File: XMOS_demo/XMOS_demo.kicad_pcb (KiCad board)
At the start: 2 copper layers, 100 x 100 mm, 128 parts, among them J1 XSYS2 DEBUG CONNECTOR, J2 USB_C_Receptacle_USB2.0_16P, J3 AudioJack3_SwitchT, U1 U316-1024-QF60B, U2 CS4271, U3 AP61200Z6, U4 TPD3S014, U5 MAX97220C, U6 W25Q32JVSS, Y1 Crystal_24M, Y2 24.576M

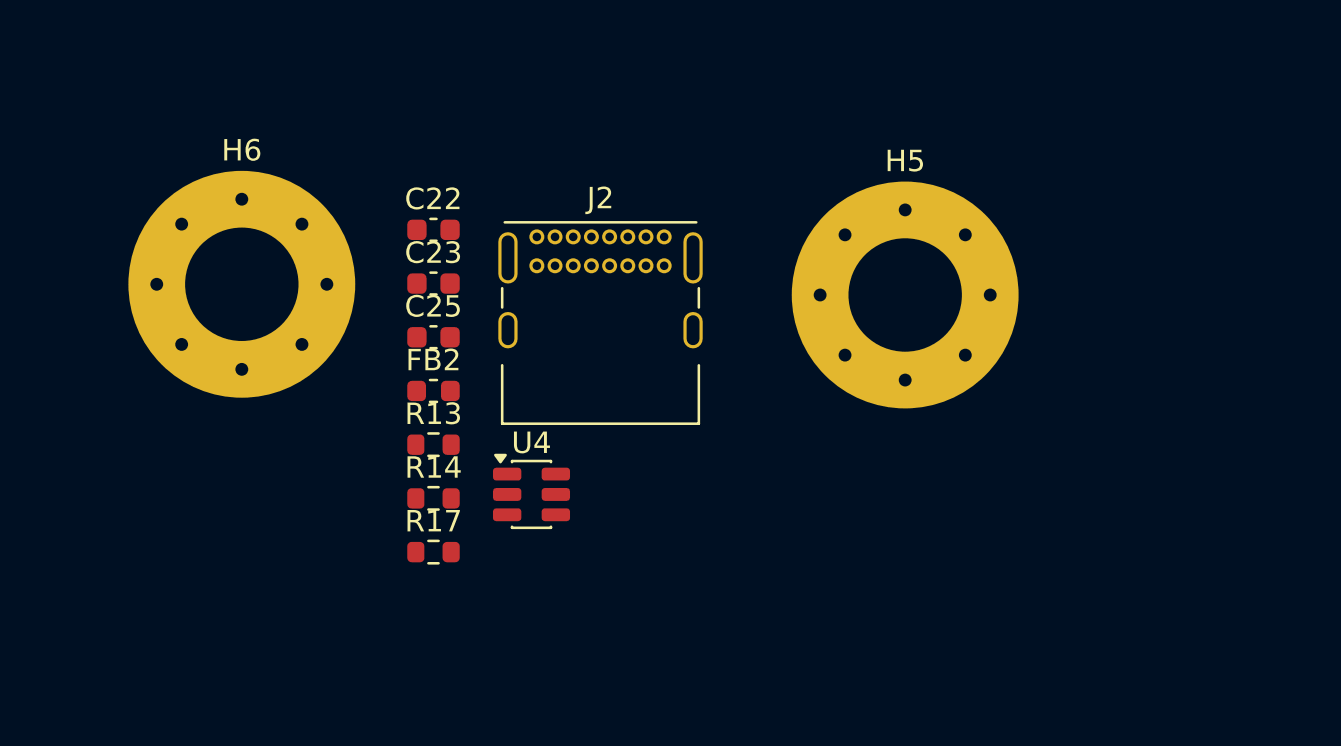
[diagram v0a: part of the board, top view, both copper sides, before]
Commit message: terminal block for power input added
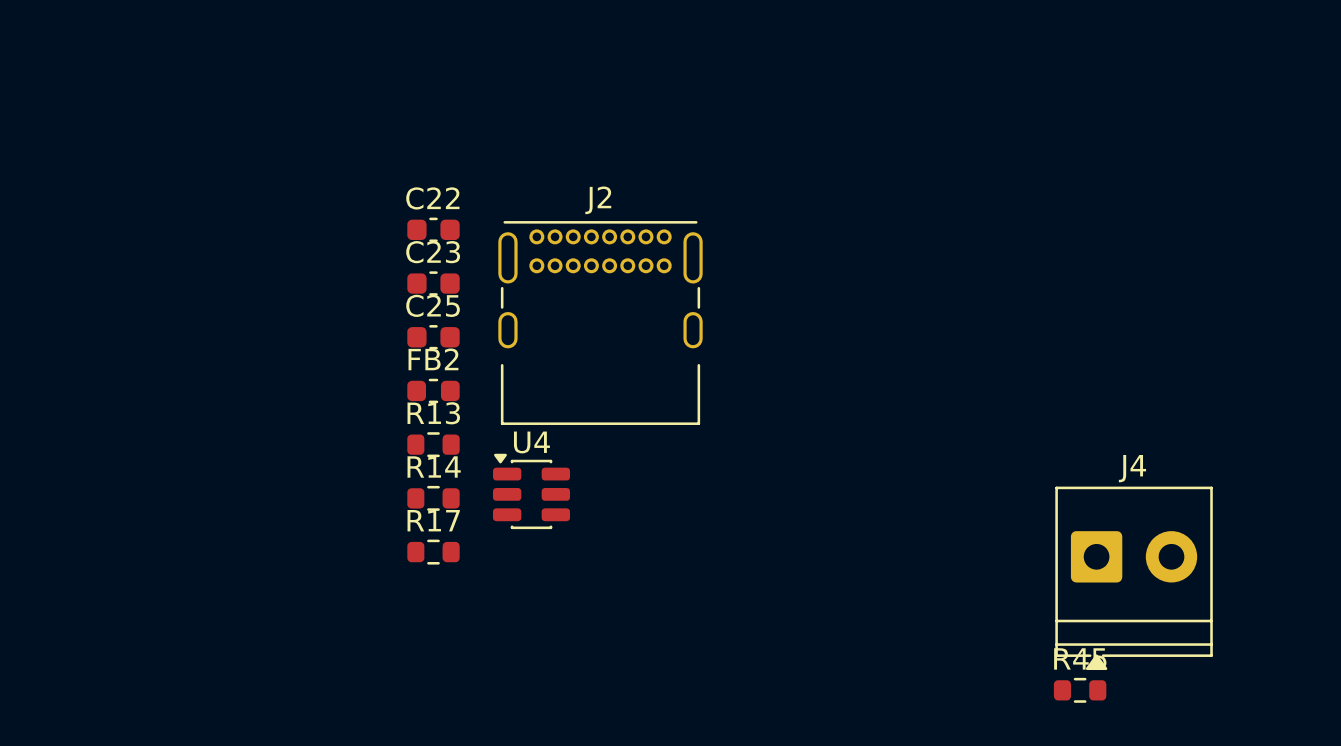
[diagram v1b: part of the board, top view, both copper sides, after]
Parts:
- removed H5: VBUS, MountingHole:MountingHole_5.3mm_M5_Pad_Via
- removed H6: GND, MountingHole:MountingHole_5.3mm_M5_Pad_Via
- added J4: Screw_Terminal_P3.50mm, TerminalBlock_Phoenix:TerminalBlock_Phoenix_PT-1,5-2-3.5-H_1x02_P3.50mm_Horizontal, F.Cu at (161.9, 181.8)
- added R45: 0R3, Resistor_SMD:R_0603_1608Metric, F.Cu at (161.2, 188.0)

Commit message: sch mostly finished, needs tp, pcb component layout started
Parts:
- removed the R17 at (131.0, 181.5)
- added C24: 22u, Capacitor_SMD:C_1206_3216Metric, F.Cu at (223.4, 126.6)
- added C26: 22u, Capacitor_SMD:C_1206_3216Metric, F.Cu at (222.4, 140.1)
- added C27: 22u, Capacitor_SMD:C_1206_3216Metric, F.Cu at (229.4, 140.1)
- added C57: 470p, Capacitor_SMD:C_0603_1608Metric, F.Cu at (82.2, 42.7)
- added C58: 2n7, Capacitor_SMD:C_0603_1608Metric, F.Cu at (43.2, 99.7)
- added C59: 1u, Capacitor_SMD:CP_Elec_4x5.4, F.Cu at (73.7, 42.0)
- added C60: 2n7, Capacitor_SMD:C_0603_1608Metric, F.Cu at (41.7, 99.2)
- added C61: 1u, Capacitor_SMD:CP_Elec_4x5.4, F.Cu at (91.0, 42.2)
- added C62: 470p, Capacitor_SMD:C_0603_1608Metric, F.Cu at (99.2, 42.7)
- added C63: 100n, Capacitor_SMD:C_0603_1608Metric, F.Cu at (80.7, 42.7)
- added C64: 100n, Capacitor_SMD:C_0603_1608Metric, F.Cu at (45.7, 104.2)
- added C65: 100n, Capacitor_SMD:C_0603_1608Metric, F.Cu at (97.7, 42.7)
- added J5: AudioJack2_SwitchT, _Connector_Audio:Jack_3.5mm_CUI_MJ-3523-SMT-TR_Horizontal, F.Cu at (77.2, 26.7)
- added J6: AudioJack2_SwitchT, _Connector_Audio:Jack_3.5mm_CUI_MJ-3523-SMT-TR_Horizontal, F.Cu at (94.7, 26.7)
- added J7: Conn_01x02_Pin, Connector_PinHeader_2.54mm:PinHeader_1x02_P2.54mm_Vertical, F.Cu at (181.2, 147.1)
- added J9: Conn_01x05, Connector_PinHeader_2.54mm:PinHeader_1x05_P2.54mm_Vertical, F.Cu at (245.2, 124.5)
- added R19: 0R, Resistor_SMD:R_0603_1608Metric, F.Cu at (150.3, 138.1)
- added R22: 0R, Resistor_SMD:R_0603_1608Metric, F.Cu at (221.4, 127.4)
- added R23: 0R, Resistor_SMD:R_0603_1608Metric, F.Cu at (220.4, 140.9)
- added R24: 0R, Resistor_SMD:R_0603_1608Metric, F.Cu at (220.0, 157.2)
- added R49: 91R, Resistor_SMD:R_0603_1608Metric, F.Cu at (83.7, 42.7)
- added R50: 634R, Resistor_SMD:R_0603_1608Metric, F.Cu at (82.9, 45.2)
- added R51: 10k, Resistor_SMD:R_0603_1608Metric, F.Cu at (81.7, 40.2)
- added R52: 10k, Resistor_SMD:R_0603_1608Metric, F.Cu at (98.7, 40.2)
- added R53: 91R, Resistor_SMD:R_0603_1608Metric, F.Cu at (100.7, 42.7)
- added R54: 634R, Resistor_SMD:R_0603_1608Metric, F.Cu at (99.7, 45.2)
- added TP1: GND, TestPoint:TestPoint_Bridge_Pitch2.54mm_Drill1.0mm, F.Cu at (140.7, 54.4)
- added TP2: GND, TestPoint:TestPoint_Bridge_Pitch2.54mm_Drill1.0mm, F.Cu at (143.4, 148.8)
- added TP3: GND, TestPoint:TestPoint_Bridge_Pitch2.54mm_Drill1.0mm, F.Cu at (94.7, 103.7)
- added TP4: GND, TestPoint:TestPoint_Bridge_Pitch2.54mm_Drill1.0mm, F.Cu at (186.3, 101.6)
- added U10: OPA340NA, Package_TO_SOT_SMD:SOT-23-5, F.Cu at (43.2, 103.7)
- added U11: OPA340NA, Package_TO_SOT_SMD:SOT-23-5, F.Cu at (95.2, 42.2)
- added U4: TLV75733PDBV, Package_TO_SOT_SMD:SOT-23-5, F.Cu at (227.1, 126.5)
- added U5: TLV75718PDBV, Package_TO_SOT_SMD:SOT-23-5, F.Cu at (225.9, 140.1)
- added U9: OPA340NA, Package_TO_SOT_SMD:SOT-23-5, F.Cu at (78.2, 42.2)
- C22, C23: value 100n -> 1u
- C25: value 100n -> 22u; footprint Capacitor_SMD:C_0603_1608Metric -> Capacitor_SMD:C_1206_3216Metric
- J2: renamed from J4; value Screw_Terminal_P3.50mm -> Screw_Terminal
- moved R41 357.3 mm to (18.7, 91.0), turned to -90 degrees
- moved R44 354.7 mm to (17.2, 91.0), turned to -90 degrees
- moved Y2 351.7 mm to (28.7, 83.7)
- moved R42 350.7 mm to (21.2, 88.7)
- moved R45 350.7 mm to (21.2, 93.2)
- moved R43 350.7 mm to (21.2, 90.2)
- moved R46 349.5 mm to (26.7, 100.2), turned to 90 degrees
- moved U8 348.6 mm to (33.7, 92.7)
- moved R47 347.9 mm to (28.2, 100.2), turned to -90 degrees
- moved R48 347.3 mm to (24.7, 83.7), turned to -90 degrees
- moved R40 346.7 mm to (21.2, 87.2)
- moved R38 345.4 mm to (26.7, 103.7), turned to 90 degrees
- moved C54 343.6 mm to (38.2, 102.0), turned to -90 degrees
- moved C56 341.7 mm to (26.2, 83.7), turned to 90 degrees
- moved C45 341.3 mm to (26.7, 92.2), turned to 90 degrees
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- renumbered C51 to C1, C8 to C10, C17 to C11, C18 to C12, C19 to C13, C13 to C14, C14 to C15, C15 to C16, C12 to C17, C10 to C18, C9 to C19, C16 to C2, C26 to C28, C11 to C29, C1 to C3, C24 to C30, C38 to C31, C28 to C32, C29 to C33, C30 to C34, C40 to C35, C41 to C36, C42 to C37, C33 to C38, C34 to C39, C2 to C4, C35 to C40, C36 to C41, C32 to C42, C27 to C43, C31 to C44, C49 to C45, C50 to C46, C48 to C47, C47 to C48, C45 to C49, C3 to C5, C46 to C50, C37 to C51, C44 to C52, C39 to C53, C43 to C54, C52 to C55, C53 to C56, C4 to C6, C5 to C7, C6 to C8, C7 to C9, D2 to D1, D3 to D2, D4 to D3, D1 to D4, J2 to J3, J3 to J4, NT2 to NT1, NT3 to NT2, NT4 to NT3, NT5 to NT4, NT1 to NT5, R10 to R1, R7 to R10, R1 to R11, R2 to R12, R3 to R13, R4 to R14, R5 to R15, R8 to R16, R9 to R17, R45 to R18, R11 to R2, R13 to R20, R14 to R21, R15 to R25, R18 to R26, R16 to R27, R19 to R28, R12 to R3, R21 to R30, R22 to R31, R23 to R32, R24 to R33, R20 to R34, R27 to R35, R26 to R36, R40 to R37, R34 to R38, R25 to R39, R35 to R4, R28 to R40, R39 to R41, R30 to R42, R31 to R43, R33 to R44, R32 to R45, R43 to R46, R44 to R47, R38 to R48, R37 to R5, R36 to R6, R41 to R7, R42 to R8, R6 to R9, U6 to U2, U4 to U3, U3 to U6, U5 to U7, U2 to U8
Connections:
- net /Codec/VQ1 renamed /Audio In/VQ1
- C22 pad 1: Net-(U4-IN) -> VBUS
- C23 pad 1: VBUS -> VBUS_FILT
- C25 pad 1: Net-(U4-IN) -> P3V3
- FB2 pad 1: Net-(U4-IN) -> VBUS_FILT
- NT1 pad 2: /Audio Out/INR+ -> /Audio Out/INL+
- NT2 pad 2: /Audio Out/INR- -> /Audio Out/INL-
- NT3 pad 2: /Audio Out/INL+ -> /Audio Out/INR+
- NT4 pad 2: /Audio Out/INL- -> /Audio Out/INR-
- U3 pad 3: Net-(U4-IN) -> VBUS_FILT
- U6 pad 5: P5V0 -> Net-(U6-EN)
- U8 pad 16: /Codec/VQ2 -> /Audio In/VQ2
- U8 pad 17: /Codec/AIN_A -> /Audio In/AIN_A
- U8 pad 18: /Codec/AIN_B -> /Audio In/AIN_B
- U8 pad 19: /Codec/VQ3 -> /Audio In/VQ2

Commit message: finished sch, pcb work
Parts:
- removed J9: Conn_01x05, Connector_PinHeader_2.54mm:PinHeader_1x05_P2.54mm_Vertical
- removed the R4 at (220.3, 94.9)
- removed the R6 at (220.3, 93.4)
- added TP5: TestPoint, TestPoint:TestPoint_Keystone_5005-5009_Compact, F.Cu at (161.5, 142.4)
- added TP6: TestPoint, TestPoint:TestPoint_Keystone_5005-5009_Compact, F.Cu at (126.4, 159.9)
- added TP7: TestPoint, TestPoint:TestPoint_Keystone_5005-5009_Compact, F.Cu at (185.8, 128.7)
- added TP8: TestPoint, TestPoint:TestPoint_Keystone_5005-5009_Compact, F.Cu at (179.3, 134.1)
- C1, C14, C15, C16: footprint Capacitor_SMD:C_0603_1608Metric -> Capacitor_SMD:C_0402_1005Metric
- C10: renamed from C11; footprint Capacitor_SMD:C_0603_1608Metric -> Capacitor_SMD:C_0402_1005Metric
- C11: renamed from C12; footprint Capacitor_SMD:C_0603_1608Metric -> Capacitor_SMD:C_0402_1005Metric
- C12: renamed from C13; footprint Capacitor_SMD:C_0603_1608Metric -> Capacitor_SMD:C_0402_1005Metric
- C13: renamed from C2; footprint Capacitor_SMD:C_0603_1608Metric -> Capacitor_SMD:C_0402_1005Metric
- C2: renamed from C3; footprint Capacitor_SMD:C_0603_1608Metric -> Capacitor_SMD:C_0402_1005Metric
- C29: footprint Capacitor_SMD:C_1206_3216Metric -> Capacitor_SMD:C_0805_2012Metric
- C3: renamed from C4; footprint Capacitor_SMD:C_0603_1608Metric -> Capacitor_SMD:C_0402_1005Metric
- C4: renamed from C5; footprint Capacitor_SMD:C_0603_1608Metric -> Capacitor_SMD:C_0402_1005Metric
- C5: renamed from C6; footprint Capacitor_SMD:C_0603_1608Metric -> Capacitor_SMD:C_0402_1005Metric
- C6: renamed from C7; footprint Capacitor_SMD:C_0603_1608Metric -> Capacitor_SMD:C_0402_1005Metric
- C7: renamed from C8; footprint Capacitor_SMD:C_0603_1608Metric -> Capacitor_SMD:C_0402_1005Metric
- C8: renamed from C9; footprint Capacitor_SMD:C_0603_1608Metric -> Capacitor_SMD:C_0402_1005Metric
- C9: renamed from C10; footprint Capacitor_SMD:C_0603_1608Metric -> Capacitor_SMD:C_0402_1005Metric
- U1: footprint _QFN:QFN-60_7x7mm_P0.4mm_EP_ThermalVias_PowerBars -> _Package_QFN:QFN-60_7x7mm_P0.4mm_EP_ThermalVias_PowerBars
- moved C25 113.0 mm to (122.9, 161.4)
- moved U4 112.9 mm to (119.7, 161.4)
- moved C24 112.5 mm to (116.5, 161.6)
- moved R20 112.5 mm to (114.5, 162.4)
- moved R42 111.6 mm to (119.3, 136.0), turned to 0 degrees
- moved R39 109.6 mm to (119.3, 134.5), turned to 0 degrees
- moved R36 107.7 mm to (132.0, 126.5), turned to 180 degrees
- moved R43 107.5 mm to (121.5, 132.0), turned to 90 degrees
- moved R37 106.0 mm to (132.0, 125.0), turned to 0 degrees
- moved R41 105.9 mm to (118.5, 132.0), turned to 90 degrees
- moved R44 105.1 mm to (128.5, 126.5), turned to 180 degrees
- moved R40 105.1 mm to (117.0, 132.0), turned to 90 degrees
- moved R38 104.4 mm to (115.5, 132.0), turned to 90 degrees
- moved R45 103.3 mm to (128.5, 125.0), turned to 0 degrees
- moved C47 101.7 mm to (123.5, 126.5), turned to 0 degrees
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- renumbered J7 to J3, J3 to J4, J4 to J5, J5 to J6, J6 to J7, R12 to R10, R13 to R11, R14 to R12, R15 to R13, R16 to R14, R17 to R15, R18 to R16, R19 to R17, R20 to R18, R21 to R19, R22 to R20, R23 to R21, R24 to R22, R25 to R23, R26 to R24, R27 to R25, R28 to R26, R29 to R27, R30 to R28, R31 to R29, R32 to R30, R33 to R31, R34 to R32, R35 to R33, R36 to R34, R37 to R35, R38 to R36, R39 to R37, R40 to R38, R41 to R39, R5 to R4, R42 to R40, R43 to R41, R44 to R42, R45 to R43, R46 to R44, R47 to R45, R48 to R46, R49 to R47, R50 to R48, R51 to R49, R7 to R5, R52 to R50, R53 to R51, R54 to R52, R8 to R6, R9 to R7, R10 to R8, R11 to R9
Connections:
- C1 pad 2: P_IO_L -> P3V3
- C13 pad 1: P_IO_L -> P3V3
- R36 pad 1: /Codec/CODEC_~{RST} -> /MCU/CODEC_~{RST}
- R38 pad 1: /Codec/CODEC_MCLK -> /Codec/MCLK
- R4 pad 2: P_IO_L -> P3V3
- R40 pad 1: /Codec/CODEC_LRCK -> /MCU/I2S_LRCK
- R41 pad 1: /Codec/CODEC_SCLK -> /MCU/I2S_SCLK
- R42 pad 1: /Codec/CODEC_SDOUT -> /MCU/I2S_ADC
- R43 pad 1: /Codec/CODEC_SDIN -> /MCU/I2S_DAC
- R5 pad 2: /MCU/SCL -> /Codec/SCL
- R6 pad 2: /MCU/SDA -> /Codec/SDA
- U1 pad 10: unconnected-(U1B-X1D01-Pad10) -> /MCU/I2S_LRCK
- U1 pad 11: unconnected-(U1B-X1D09-Pad11) -> /MCU/CODEC_~{RST}
- U1 pad 13: unconnected-(U1B-X1D10-Pad13) -> /MCU/I2S_SCLK
- U1 pad 14: unconnected-(U1B-X1D11-Pad14) -> /Codec/MCLK
- U1 pad 41: /MCU/SCL -> /Codec/SCL
- U1 pad 43: /MCU/SDA -> /Codec/SDA
- U1 pad 7: unconnected-(U1B-X0D11-Pad7) -> /MCU/I2S_ADC
- U1 pad 8: P_IO_L -> P3V3
- U1 pad 9: unconnected-(U1B-X1D00-Pad9) -> /MCU/I2S_DAC
- U2 pad 8: P_IO_L -> P3V3
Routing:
- net VBUS: track 0.00 -> 24.6 mm
- net P0V9: track 0.00 -> 18.7 mm
- net GND: track 0.00 -> 12.2 mm, vias 0 -> 8
- net Net-(U1C-XIN): track 0.00 -> 7.20 mm
- net P0V9A: track 0.00 -> 7.12 mm
- net Net-(J4-CC2): track 0.00 -> 6.94 mm, vias 0 -> 1
- net Net-(J2-Pin_2): track 0.00 -> 6.85 mm
- net Net-(U1C-XOUT): track 0.00 -> 6.79 mm
- net Net-(J4-CC1): track 0.00 -> 6.24 mm, vias 0 -> 1
- net /MCU/TDI: track 0.00 -> 5.83 mm
- net P1V8: track 0.00 -> 5.76 mm
- net /MCU/RST_N: track 0.00 -> 5.76 mm
- net /MCU/TDO: track 0.00 -> 5.73 mm
- net Net-(C20-Pad1): track 0.00 -> 5.54 mm
- net /MCU/TMS: track 0.00 -> 5.17 mm
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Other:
- rule pad_to_mask_clearance: 0 -> 0.1

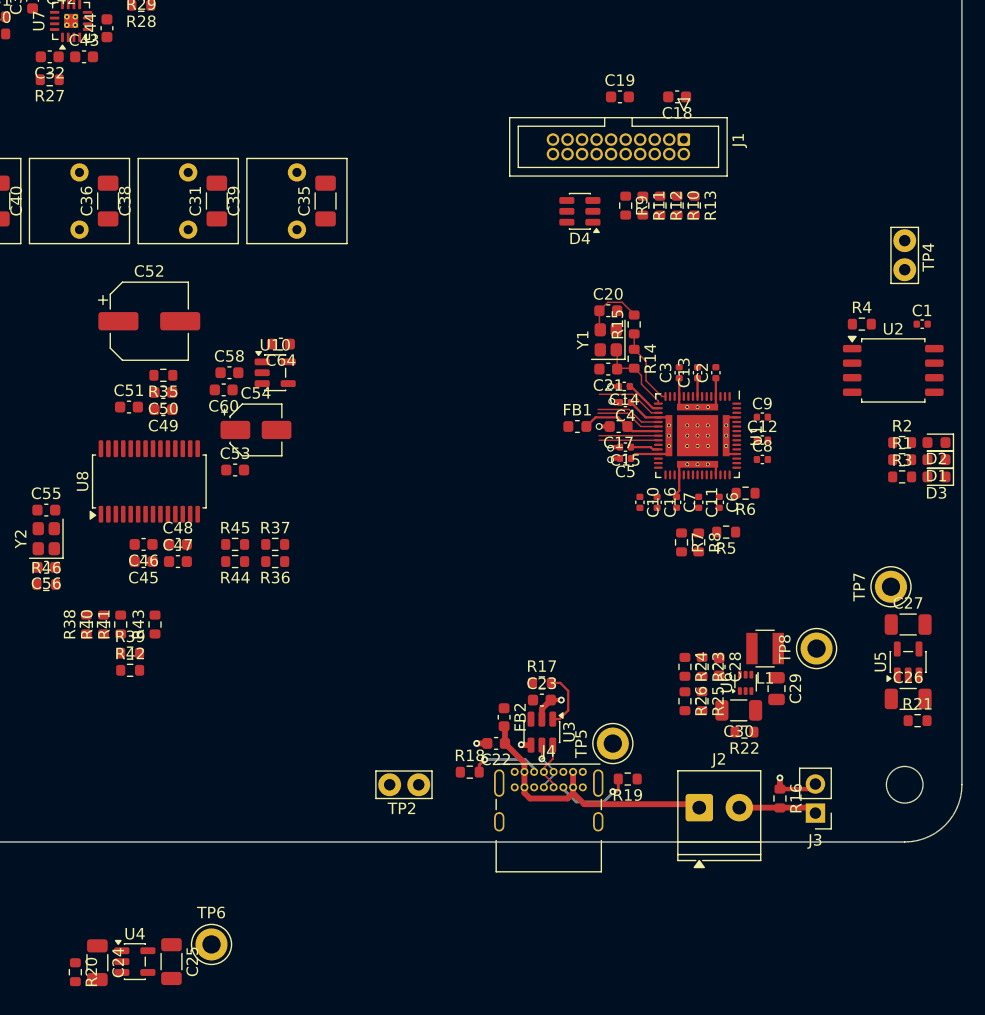
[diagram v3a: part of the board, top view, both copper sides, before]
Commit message: PCB work, changes for better routing
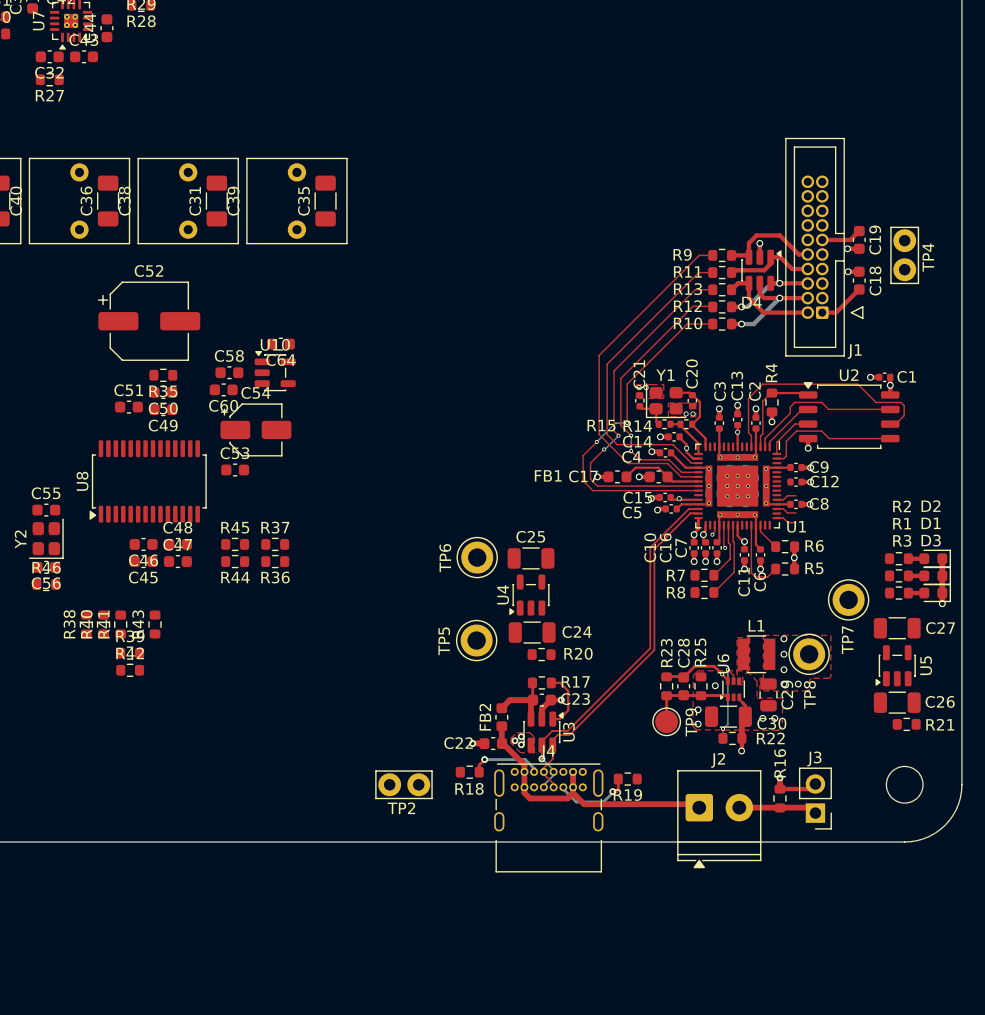
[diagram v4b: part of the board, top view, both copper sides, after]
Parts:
- removed R24: 100k, Resistor_SMD:R_0603_1608Metric
- removed R26: 200k, Resistor_SMD:R_0603_1608Metric
- added C66: 100n, Capacitor_SMD:C_0402_1005Metric, B.Cu at (170.4, 119.2)
- added C67: 100n, Capacitor_SMD:C_0402_1005Metric, B.Cu at (170.4, 120.6)
- added C68: 100n, Capacitor_SMD:C_0402_1005Metric, B.Cu at (171.7, 122.0)
- added C69: 100n, Capacitor_SMD:C_0402_1005Metric, B.Cu at (173.1, 122.0)
- added C70: 100n, Capacitor_SMD:C_0402_1005Metric, B.Cu at (174.5, 119.2)
- added C71: 100n, Capacitor_SMD:C_0402_1005Metric, B.Cu at (174.5, 120.6)
- added C72: 100n, Capacitor_SMD:C_0402_1005Metric, B.Cu at (173.1, 117.8)
- added C73: 100n, Capacitor_SMD:C_0402_1005Metric, B.Cu at (171.7, 117.8)
- added TP9: TestPoint, TestPoint:TestPoint_Pad_D2.0mm, F.Cu at (166.2, 140.5)
- C20, C21: footprint Capacitor_SMD:C_0603_1608Metric -> Capacitor_SMD:C_0402_1005Metric
- R14, R15: footprint Resistor_SMD:R_0603_1608Metric -> Resistor_SMD:R_0402_1005Metric
- moved R20 49.3 mm to (155.3, 134.6), turned to 0 degrees
- moved C24 47.7 mm to (154.4, 132.7), turned to 0 degrees
- moved C25 47.2 mm to (154.3, 126.2), turned to 0 degrees
- moved U4 47.2 mm to (154.3, 129.4), turned to 90 degrees
- moved TP6 41.0 mm to (149.7, 126.2), turned to 90 degrees
- moved C19 24.4 mm to (183.0, 98.4), turned to -90 degrees
- moved C18 22.6 mm to (183.0, 102.0), turned to 90 degrees
- moved J1 19.3 mm to (179.2, 99.0), turned to 180 degrees
- moved D4 16.5 mm to (174.3, 101.0), turned to -90 degrees
- moved TP5 14.9 mm to (149.6, 133.4), turned to -90 degrees
- moved R10 11.1 mm to (171.0, 105.8), turned to 180 degrees
- moved C20 10.8 mm to (168.4, 112.4), turned to -90 degrees
- moved R4 10.4 mm to (175.4, 112.6), turned to -90 degrees
- moved R12 10.4 mm to (171.1, 104.2), turned to 180 degrees
- moved D1 10.2 mm to (189.5, 127.8)
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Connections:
- net Net-(U6-SW) renamed /POWER SUPPLY/SW
- C20 pad 1: Net-(C20-Pad1) -> Net-(U1C-XOUT)
- C21 pad 1: Net-(U1C-XIN) -> Net-(C21-Pad1)
- D4 pad 1: /MCU/XTAG_RST_N -> /MCU/XTAG_TDI
- D4 pad 3: /MCU/XTAG_TCK -> /MCU/XTAG_RST_N
- D4 pad 4: /MCU/XTAG_TDI -> /MCU/XTAG_TMS
- D4 pad 5: /MCU/XTAG_TDO -> /MCU/XTAG_TCK
- D4 pad 6: /MCU/XTAG_TMS -> /MCU/XTAG_TDO
- R15 pad 1: Net-(U1C-XOUT) -> Net-(U1C-XIN)
- R15 pad 2: Net-(C20-Pad1) -> Net-(C21-Pad1)
- Y1 pad 1: Net-(U1C-XIN) -> Net-(C21-Pad1)
- Y1 pad 3: Net-(C20-Pad1) -> Net-(U1C-XOUT)
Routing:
- net /USB/USBD-: track 4.49 -> 32.1 mm
- net /MCU/TMS: track 5.17 -> 31.9 mm, vias 0 -> 2
- net /USB/USBD+: track 4.36 -> 30.9 mm
- net /MCU/TCK: track 5.17 -> 30.7 mm, vias 0 -> 2
- net /MCU/RST_N: track 5.76 -> 30.7 mm
- net /MCU/TDI: track 5.83 -> 27.7 mm
- net /MCU/QSPI_CLK: track 0.00 -> 21.6 mm
- net /MCU/TDO: track 5.73 -> 24.0 mm, vias 0 -> 2
- net GND: track 12.2 -> 29.2 mm, vias 8 -> 34
- net /MCU/QSPI_D3: track 0.00 -> 13.5 mm
- net P3V3: track 1.59 -> 14.0 mm, vias 0 -> 6
- net /MCU/QSPI_D0: track 0.00 -> 11.9 mm
- net P0V9: track 18.7 -> 29.9 mm, vias 0 -> 7
- net /MCU/XTAG_TCK: track 0.00 -> 10.4 mm, vias 0 -> 2
- net /MCU/XTAG_TMS: track 0.00 -> 8.70 mm
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- added copper zone on F.Cu, net /POWER SUPPLY/SW
- added copper zone on F.Cu, net GND
- added copper zone on F.Cu, net P0V9
- added copper zone on F.Cu, net P5V0
